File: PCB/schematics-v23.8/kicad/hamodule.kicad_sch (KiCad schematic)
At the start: 137 parts, among them J1 GND|5V, J10 Tx|Rx, J11 USB_C_Receptacle_USB2.0, J12 2604-1104, J14 2604-1104, J15 2604-1104, J2 2604-1102, J3 Sda|Scl, J4 13|12, J5 9|3|16, J6 GND|3.3V, J7 Conn_01x02_Pin, J9 2604-1104, K1 AQG12205, K2 AQG12205, K3 AQG12205, K4 AQG12205, K5 AQG12205, K6 AQG12205, K7 AQG12205, K8 AQG12205, SW1 Switch, SW2 Switch, SW3 USB | PS, U1 LD1117AV33, U10 ULN2803A, U2 ESP32-S3-WROOM-2, U3 LDA210-PDIP, U4 USBLC6-2SC6, U5 LDA210-PDIP, U6 LDA210-PDIP, U7 SHT4x, U8 LDA210-PDIP, U9 MCP23017_SO

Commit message: not sure what changed :(
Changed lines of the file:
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@@
     (stroke (width 0) (type default))
   )
+  (wire (pts (xy 285.115 135.89) (xy 285.115 137.795))
+    (stroke (width 0) (type default))
+  )
   (wire (pts (xy 212.09 61.595) (xy 209.55 61.595))
     (stroke (width 0) (type default))
@@
     (data
       iVBORw0KGgoAAAANSUhEUgAAAngAAAMbCAIAAABR4n8tAAAAA3NCSVQICAjb4U/gAAAACXBIWXMA
-      AA7DAAAOwwHHb6hkAAAgAElEQVR4nGy9Xa8kSXIldo6Ze0Tee6uqP2aaHHFFailSggBRD4L0P7S7
+      AA50AAAOdAFrJLPWAAAgAElEQVR4nGy9Xa8kSXIldo6Ze0Tee6uqP2aaHHFFailSggBRD4L0P7S7
       5Epa/UBBz/oPAgQsBAh8ECVitSuI3OH0TE9XdVXdezPC3cz0YO6eWU1lNwp5MyMjPNzN7Zgd+wj+
       z//T/2hmtdbjOMpW3Z0kgPFvwN3NDICIAFhveu+OEBFVVdU8hoGIcPeIAKCqEALIP0mKiJmtU60T
@@
     )
   )
-  (global_label "GND" (shape input) (at 286.385 135.89 270) (fields_autoplaced)
+  (global_label "GND" (shape input) (at 285.115 137.795 270) (fields_autoplaced)
     (effects (font (size 1.27 1.27)) (justify right))
-    (property "Intersheetrefs" "${INTERSHEET_REFS}" (at 234.315 360.68 0)
+    (property "Intersheetrefs" "${INTERSHEET_REFS}" (at 233.045 362.585 0)
       (effects (font (size 1.27 1.27)) hide)
     )

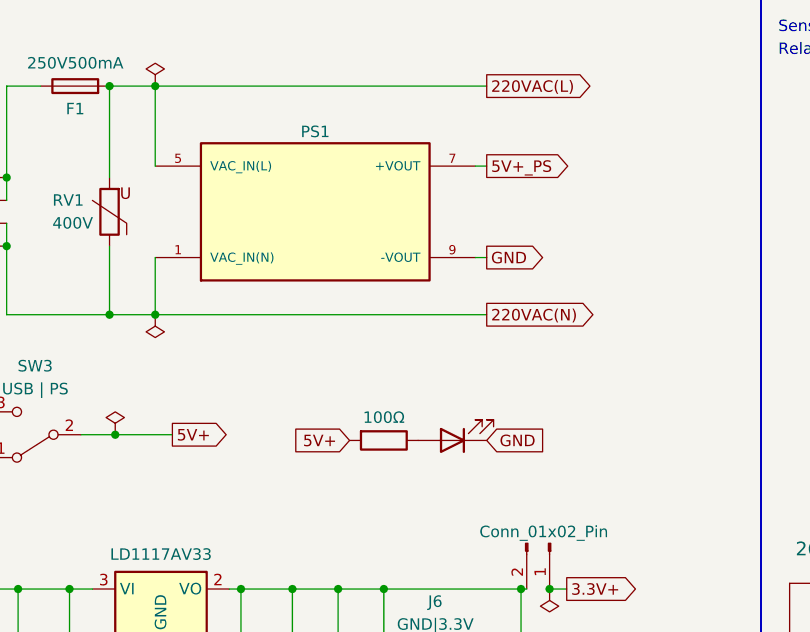
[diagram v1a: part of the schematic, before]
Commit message: [V8] adding indicators for 5 and 3.3 V
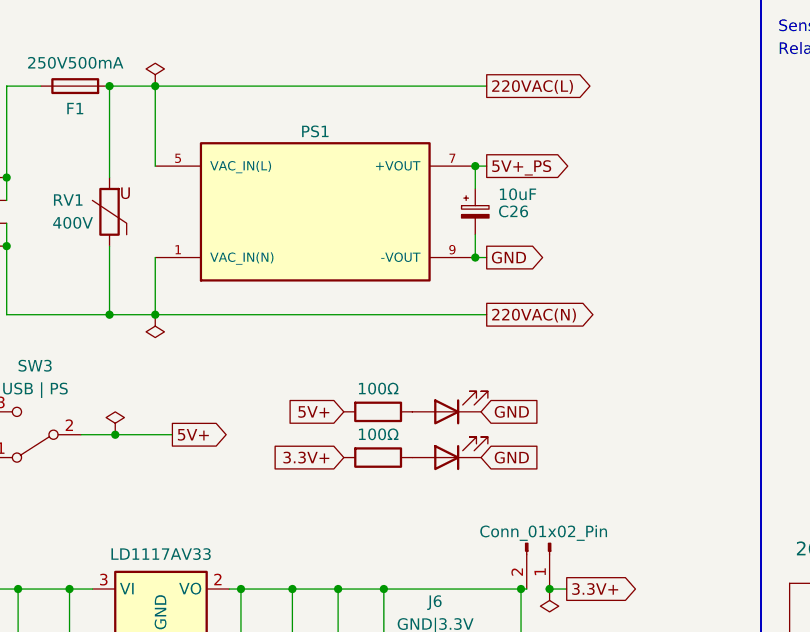
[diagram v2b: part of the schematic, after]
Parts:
- added C26: 10uF, Capacitor_THT:CP_Radial_D6.3mm_P2.50mm, symbol Device:C_Polarized_Small
- added D12: 3.3V, LED_SMD:LED_0805_2012Metric_Pad1.15x1.40mm_HandSolder, symbol Device:LED
- added R44: 100Ω, Resistor_SMD:R_0805_2012Metric_Pad1.20x1.40mm_HandSolder, symbol Device:R
- D1: value LED -> 5V
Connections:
- net 3.3V+: now also R44.2
- net 5V+_PS: now also C26.1
- net GND: now also C26.2, D12.1 (K)
- new net: D12.2 (A), R44.1
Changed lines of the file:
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@@
   (junction (at 151.13 142.875) (diameter 0) (color 0 0 0 0)
   )
+  (junction (at 102.87 31.75) (diameter 0) (color 0 0 0 0)
+  )
   (junction (at 87.63 78.74) (diameter 0) (color 0 0 0 0)
   )
@@
   (junction (at 393.065 149.225) (diameter 0) (color 0 0 0 0)
   )
+  (junction (at 102.87 41.91) (diameter 0) (color 0 0 0 0)
+  )
   (junction (at 69.215 125.095) (diameter 0) (color 0 0 0 0)
   )
@@
     (stroke (width 0) (type default))
   )
+  (wire (pts (xy 102.87 39.37) (xy 102.87 41.91))
+    (stroke (width 0) (type default))
+  )
   (wire (pts (xy 153.035 83.185) (xy 156.845 83.185))
     (stroke (width 0) (type default))
@@
     (stroke (width 0) (type default))
   )
+  (wire (pts (xy 102.87 31.75) (xy 102.87 34.29))
+    (stroke (width 0) (type default))
+  )
   (wire (pts (xy 111.125 78.74) (xy 113.03 78.74))
     (stroke (width 0) (type default))
@@
     )
   )
+  (global_label "3.3V+" (shape input) (at 88.265 64.135 180) (fields_autoplaced)
+    (effects (font (size 1.27 1.27)) (justify right))
+    (property "Intersheetrefs" "${INTERSHEET_REFS}" (at 80.3286 64.135 0)
+      (effects (font (size 1.27 1.27)) (justify right) hide)
+    )
+  )
   (global_label "SDA" (shape input) (at 346.075 217.805 90) (fields_autoplaced)
     (effects (font (size 1.27 1.27)) (justify left))
@@
     )
   )
-  (global_label "5V+" (shape input) (at 88.9 62.23 180) (fields_autoplaced)
+  (global_label "5V+" (shape input) (at 88.265 59.055 180) (fields_autoplaced)
     (effects (font (size 1.27 1.27)) (justify right))
-    (property "Intersheetrefs" "${INTERSHEET_REFS}" (at 124.46 113.03 0)
+    (property "Intersheetrefs" "${INTERSHEET_REFS}" (at 123.825 109.855 0)
       (effects (font (size 1.27 1.27)) hide)
     )
@@
     )
   )
-  (global_label "GND" (shape input) (at 104.14 62.23 0) (fields_autoplaced)
+  (global_label "GND" (shape input) (at 103.505 59.055 0) (fields_autoplaced)
     (effects (font (size 1.27 1.27)) (justify left))
-    (property "Intersheetrefs" "${INTERSHEET_REFS}" (at 328.93 114.3 0)
+    (property "Intersheetrefs" "${INTERSHEET_REFS}" (at 328.295 111.125 0)
       (effects (font (size 1.27 1.27)) hide)
     )
@@
     )
   )
+  (global_label "GND" (shape input) (at 103.505 64.135 0) (fields_autoplaced)
+    (effects (font (size 1.27 1.27)) (justify left))
+    (property "Intersheetrefs" "${INTERSHEET_REFS}" (at 328.295 116.205 0)
+      (effects (font (size 1.27 1.27)) hide)
+    )
+  )
   (global_label "220VAC(L)" (shape input) (at 359.41 160.655 0) (fields_autoplaced)
     (effects (font (size 1.27 1.27)) (justify left))
@@
     )
   )
-  (symbol (lib_id "Device:R") (at 92.71 62.23 270) (unit 1)
+  (symbol (lib_id "Device:R") (at 92.075 59.055 270) (unit 1)
     (in_bom yes) (on_board yes) (dnp no)
-    (property "Reference" "R2" (at 96.52 55.88 90)
+    (property "Reference" "R2" (at 95.885 52.705 90)
       (effects (font (size 1.27 1.27)) hide)
     )
-    (property "Value" "100Ω" (at 92.71 59.69 90)
+    (property "Value" "100Ω" (at 92.075 56.515 90)
       (effects (font (size 1.27 1.27)))
     )
-    (property "Footprint" "Resistor_SMD:R_0805_2012Metric_Pad1.20x1.40mm_HandSolder" (at 92.71 60.452 90)
+    (property "Footprint" "Resistor_SMD:R_0805_2012Metric_Pad1.20x1.40mm_HandSolder" (at 92.075 57.277 90)
       (effects (font (size 1.27 1.27)) hide)
     )
-    (property "Datasheet" "https://www.distrelec.ch/en/high-power-thick-film-smd-resistor-0805-150ohm-330mw-rnd-components-rnd-155hp05w3f1500t5e/p/30111774?q=*&pos=2&origPos=1787&origPageSize=50&track=true" (at 92.71 62.23 0)
+    (property "Datasheet" "https://www.distrelec.ch/en/high-power-thick-film-smd-resistor-0805-150ohm-330mw-rnd-components-rnd-155hp05w3f1500t5e/p/30111774?q=*&pos=2&origPos=1787&origPageSize=50&track=true" (at 92.075 59.055 0)
       (effects (font (size 1.27 1.27)) hide)
     )
-    (property "JLCPCB" "C17408" (at 92.71 62.23 0)
+    (property "JLCPCB" "C17408" (at 92.075 59.055 0)
       (effects (font (size 1.27 1.27)) hide)
     )
-    (property "LCSC" "C17408" (at 92.71 62.23 0)
+    (property "LCSC" "C17408" (at 92.075 59.055 0)
       (effects (font (size 1.27 1.27)) hide)
     )
@@
     )
   )
-  (symbol (lib_id "Device:LED") (at 100.33 62.23 180) (unit 1)
+  (symbol (lib_id "Device:LED") (at 99.695 59.055 180) (unit 1)
     (in_bom yes) (on_board yes) (dnp no)
-    (property "Reference" "D1" (at 97.79 71.12 0)
+    (property "Reference" "D1" (at 97.155 67.945 0)
       (effects (font (size 1.27 1.27)) hide)
     )
-    (property "Value" "LED" (at 96.52 60.96 0)
+    (property "Value" "5V" (at 95.885 57.785 0)
       (effects (font (size 1.27 1.27)) hide)
     )
-    (property "Footprint" "LED_SMD:LED_0805_2012Metric_Pad1.15x1.40mm_HandSolder" (at 100.33 62.23 0)
+    (property "Footprint" "LED_SMD:LED_0805_2012Metric_Pad1.15x1.40mm_HandSolder" (at 99.695 59.055 0)
       (effects (font (size 1.27 1.27)) hide)
     )
-    (property "Datasheet" "https://www.distrelec.ch/en/smd-led-green-575nm-20ma-2v-140-everlight-electronics-17-21sygc-s530-e1-tr8/p/17531205?q=*&pos=9&origPos=371&origPageSize=50&track=true" (at 100.33 62.23 0)
+    (property "Datasheet" "https://www.distrelec.ch/en/smd-led-green-575nm-20ma-2v-140-everlight-electronics-17-21sygc-s530-e1-tr8/p/17531205?q=*&pos=9&origPos=371&origPageSize=50&track=true" (at 99.695 59.055 0)
       (effects (font (size 1.27 1.27)) hide)
     )
-    (property "JLCPCB" "C2297" (at 100.33 62.23 0)
+    (property "JLCPCB" "C2297" (at 99.695 59.055 0)
       (effects (font (size 1.27 1.27)) hide)
     )
-    (property "LCSC" "C2297" (at 100.33 62.23 0)
+    (property "LCSC" "C2297" (at 99.695 59.055 0)
       (effects (font (size 1.27 1.27)) hide)
     )
+    (property "PcbText" "" (at 99.695 59.055 0)
+      (effects (font (size 1.27 1.27)))
+    )
     (pin "1")
     (pin "2")
@@
     )
   )
+  (symbol (lib_id "Device:R") (at 92.075 64.135 270) (unit 1)
+    (in_bom yes) (on_board yes) (dnp no)
+    (property "Reference" "R44" (at 95.885 57.785 90)
+      (effects (font (size 1.27 1.27)) hide)
+    )
+    (property "Value" "100Ω" (at 92.075 61.595 90)
+      (effects (font (size 1.27 1.27)))
+    )
+    (property "Footprint" "Resistor_SMD:R_0805_2012Metric_Pad1.20x1.40mm_HandSolder" (at 92.075 62.357 90)
+      (effects (font (size 1.27 1.27)) hide)
+    )
+    (property "Datasheet" "https://www.distrelec.ch/en/high-power-thick-film-smd-resistor-0805-150ohm-330mw-rnd-components-rnd-155hp05w3f1500t5e/p/30111774?q=*&pos=2&origPos=1787&origPageSize=50&track=true" (at 92.075 64.135 0)
+      (effects (font (size 1.27 1.27)) hide)
+    )
+    (property "JLCPCB" "C17408" (at 92.075 64.135 0)
+      (effects (font (size 1.27 1.27)) hide)
+    )
+    (property "LCSC" "C17408" (at 92.075 64.135 0)
+      (effects (font (size 1.27 1.27)) hide)
+    )
+    (pin "1")
+    (pin "2")
+    (instances
+      (project "hamodule"
+        (path "/e5217a0c-7f55-4c30-adda-7f8d95709d1b"
+          (reference "R44") (unit 1)
+        )
+      )
+    )
+  )
   (symbol (lib_id "Device:R") (at 209.55 94.615 0) (unit 1)
     (in_bom yes) (on_board yes) (dnp no)
@@
     )
   )
+  (symbol (lib_id "Device:C_Polarized_Small") (at 102.87 36.83 0) (unit 1)
+    (in_bom yes) (on_board yes) (dnp no)
+    (property "Reference" "C26" (at 105.41 36.83 0)
+      (effects (font (size 1.27 1.27)) (justify left))
+    )
+    (property "Value" "10uF" (at 105.41 34.925 0)
+      (effects (font (size 1.27 1.27)) (justify left))
+    )
+    (property "Footprint" "Capacitor_THT:CP_Radial_D6.3mm_P2.50mm" (at 103.8352 40.64 0)
+      (effects (font (size 1.27 1.27)) hide)
+    )
+    (property "Datasheet" "~" (at 102.87 36.83 0)
+      (effects (font (size 1.27 1.27)) hide)
+    )
+    (pin "1")
+    (pin "2")
+    (instances
+      (project "hamodule"
+        (path "/e5217a0c-7f55-4c30-adda-7f8d95709d1b"
+          (reference "C26") (unit 1)
+        )
+      )
+    )
+  )
   (symbol (lib_id "Diode:BAT60A") (at 94.615 118.745 180) (unit 1)
     (in_bom yes) (on_board yes) (dnp no)
@@
         )
       )
+    )
+  )
+  (symbol (lib_id "Device:LED") (at 99.695 64.135 180) (unit 1)
+    (in_bom yes) (on_board yes) (dnp no)
+    (property "Reference" "D12" (at 97.155 73.025 0)
+      (effects (font (size 1.27 1.27)) hide)
+    )
+    (property "Value" "3.3V" (at 95.885 62.865 0)
+      (effects (font (size 1.27 1.27)) hide)
+    )
+    (property "Footprint" "LED_SMD:LED_0805_2012Metric_Pad1.15x1.40mm_HandSolder" (at 99.695 64.135 0)
+      (effects (font (size 1.27 1.27)) hide)
+    )
+    (property "Datasheet" "https://www.distrelec.ch/en/smd-led-green-575nm-20ma-2v-140-everlight-electronics-17-21sygc-s530-e1-tr8/p/17531205?q=*&pos=9&origPos=371&origPageSize=50&track=true" (at 99.695 64.135 0)
+      (effects (font (size 1.27 1.27)) hide)
+    )
+    (property "JLCPCB" "C2297" (at 99.695 64.135 0)
+      (effects (font (size 1.27 1.27)) hide)
+    )
+    (property "LCSC" "C2297" (at 99.695 64.135 0)
+      (effects (font (size 1.27 1.27)) hide)
+    )
+    (property "PcbText" "" (at 99.695 64.135 0)
+      (effects (font (size 1.27 1.27)))
+    )
+    (pin "1")
+    (pin "2")
+    (instances
+      (project "hamodule"
+        (path "/e5217a0c-7f55-4c30-adda-7f8d95709d1b"
+          (reference "D12") (unit 1)
+        )
+      )

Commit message: [V8] fixing switch silkscreen
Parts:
- SW1: value Switch -> Reset
- SW2: value Switch -> Boot
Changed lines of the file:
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@@
   (title_block
     (title "Home Assistant module for lights control")
-    (date "2023-02-01")
-    (rev "20230201.22")
+    (date "2023-09-26")
+    (rev "20230926.22")
   )
   (junction (at 290.195 135.89) (diameter 0) (color 0 0 0 0)
@@
       (effects (font (size 1.27 1.27)))
     )
-    (property "Value" "Switch" (at 98.425 158.2674 0)
+    (property "Value" "Reset" (at 98.425 158.2674 0)
       (effects (font (size 1.27 1.27)) hide)
     )
@@
       (effects (font (size 1.27 1.27)))
     )
-    (property "Value" "Switch" (at 98.425 164.6174 0)
+    (property "Value" "Boot" (at 98.425 164.6174 0)
       (effects (font (size 1.27 1.27)) hide)
     )
